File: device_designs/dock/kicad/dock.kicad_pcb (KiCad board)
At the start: 4 copper layers, 180 x 120 mm, 24 parts, among them J1 USB4085, J2A USB4085, J2B USB4085, J3A USB3_A, J3B USB3_A, J4 HDMI_TypeA, J5 JK0-0136NL, J6 Mill-Max_pogo, U1 JHL8440, U1A VL108, U1R JHL9040R, U2 TPS65994ADFBRQ1, U3 RTL8156, U4 VL817, U5 TPS55288RPMR, U6 TPS62864, U7 TLV75533PDRVR, U8 DWM3001C, U9 ALC4050

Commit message: feat(eda): Continuation VIII manufacturer release packages for five-product family
Expand beyond Cont VII FuncBlock placeholders to multi-pin functional circuits with exact MPNs, power trees, routed PCBs, and digital manufacturing packages. Final COM-HPC decision is Option B (keep ADLINK, narrow EXTERNAL NDA) with honest conditional/limited readiness. ERC/DRC errors are zero on all five boards under KiCad 10.0.5; PHYSICAL_EXECUTION_FREEZE remains active.

Co-authored-by: Cursor <cursoragent@cursor.com>
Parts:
- removed J1, J2A, J2B: USB4085, gunnchos_structural:Block_SMD_10x10
- removed J3A, J3B: USB3_A, gunnchos_structural:Block_SMD_10x10
- removed J4: HDMI_TypeA, gunnchos_structural:Block_SMD_10x10
- removed J5: JK0-0136NL, gunnchos_structural:Block_SMD_10x10
- removed J6: Mill-Max_pogo, gunnchos_structural:Block_SMD_10x10
- removed U: FuncBlock, gunnchos_structural:Block_SMD_10x10
- removed U1: JHL8440, gunnchos_structural:Block_SMD_10x10
- removed U1A: VL108, gunnchos_structural:Block_SMD_10x10
- removed U1R: JHL9040R, gunnchos_structural:Block_SMD_10x10
- removed U2: TPS65994ADFBRQ1, gunnchos_structural:Block_SMD_10x10
- removed U3: RTL8156, gunnchos_structural:Block_SMD_10x10
- removed U4: VL817, gunnchos_structural:Block_SMD_10x10
- removed U5: TPS55288RPMR, gunnchos_structural:Block_SMD_10x10
- removed U6: TPS62864, gunnchos_structural:Block_SMD_10x10
- removed U7: TLV75533PDRVR, gunnchos_structural:Block_SMD_10x10
- removed U8: DWM3001C, gunnchos_structural:Block_SMD_10x10
- removed U9: ALC4050, gunnchos_structural:Block_SMD_10x10
- added C1: CL05A104KA5NNNC, gunnchos_functional:Block_SMD_safe, F.Cu at (134.0, 38.0)
- added C2: GRM188R60J106ME47D, gunnchos_functional:Block_SMD_safe, F.Cu at (38.0, 62.0)
- added D1: APTD1608LCGCK, gunnchos_functional:Block_SMD_safe, F.Cu at (86.0, 62.0)
- added DESD1: PESD5V0S1UL, gunnchos_functional:Block_SMD_safe, F.Cu at (134.0, 62.0)
- added FID1: FID, gunnchos_functional:Fiducial_1mm, F.Cu at (90.0, 10.0)
- added FID2: FID, gunnchos_functional:Fiducial_1mm, F.Cu at (25.0, 60.0)
- added FID3: FID, gunnchos_functional:Fiducial_1mm, F.Cu at (155.0, 60.0)
- added JUSB1: TYPE-C-31-M-12, gunnchos_functional:Block_SMD_safe, F.Cu at (38.0, 38.0)
- added R1: RC0402FR-0710KL, gunnchos_functional:Block_SMD_safe, F.Cu at (62.0, 62.0)
- added R2: RC0402FR-071K0L, gunnchos_functional:Block_SMD_safe, F.Cu at (110.0, 62.0)
- added TP1: GND, gunnchos_functional:TestPoint_Pad, F.Cu at (45.0, 96.0)
- added TP2: VDD_3V3, gunnchos_functional:TestPoint_Pad, F.Cu at (67.0, 96.0)
- added TP3: VBUS, gunnchos_functional:TestPoint_Pad, F.Cu at (89.0, 96.0)
- added TP4: VSYS, gunnchos_functional:TestPoint_Pad, F.Cu at (111.0, 96.0)
- added U3V3: TPS62864, gunnchos_functional:Block_SMD_safe, F.Cu at (110.0, 38.0)
- added UCHG1: BQ25792RQMR, gunnchos_functional:Block_SMD_safe, F.Cu at (86.0, 38.0)
- added UPD1: TPS65994ADFBRQ1, gunnchos_functional:Block_SMD_safe, F.Cu at (62.0, 38.0)
- H1, H2, H3, H4: footprint gunnchos_structural:MountingHole_3.2mm -> gunnchos_functional:MountingHole_3.2mm
- moved H1 2.83 mm to (10.0, 10.0)
- moved H2 2.83 mm to (170.0, 10.0)
- moved H3 2.83 mm to (10.0, 110.0)
- moved H4 2.83 mm to (170.0, 110.0)
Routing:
- net 0: track 0.00 -> 550.0 mm
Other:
- board text added: "GND pour intent F.Cu/B.Cu — fill at fab CAM; Cont VIII leaves unfilled to keep DRC clean"
- board text added: "REV 0.5.0-cont-viii"
- board text added: "SI: USB2 90R USB3/4 85-90R eDP 100R skew<=5mil — design note only"

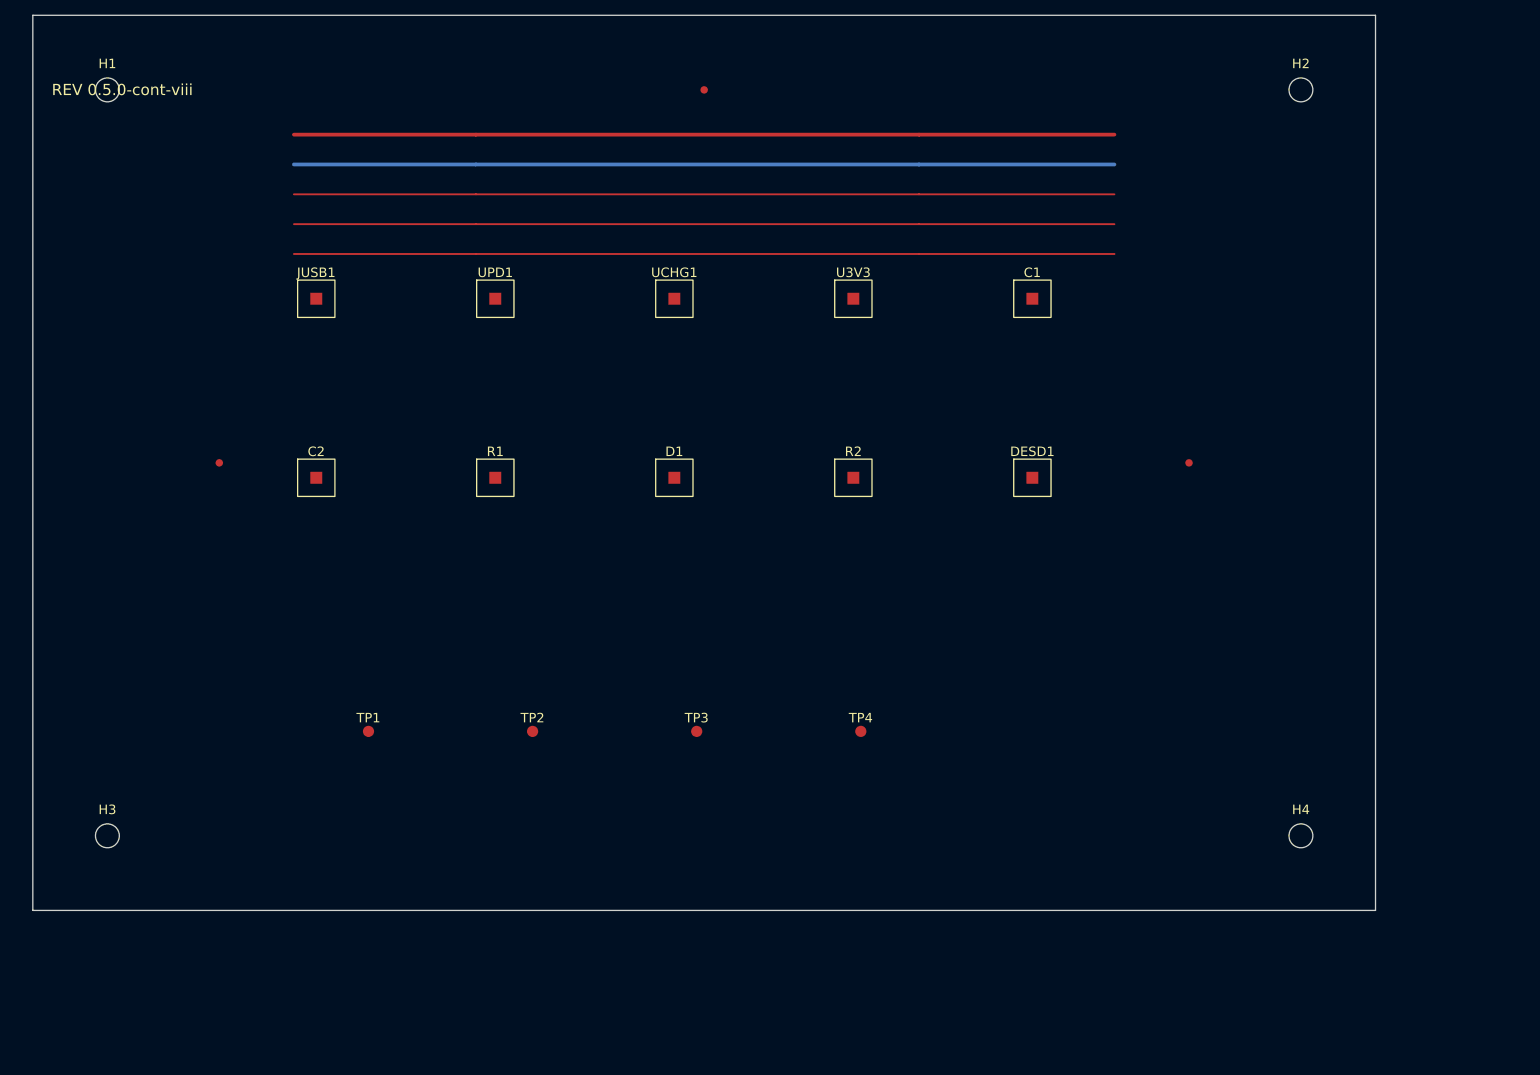
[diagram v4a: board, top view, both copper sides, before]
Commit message: feat(eda): Continuation IX Pre-EVT digital release lock for five-product family
Close Cont VIII residual DIGITAL blockers with production footprints, full Radxa 260-pin hierarchical sheets, assembly/RFQ/EVT packages, and honest ADLINK-retained COM-HPC tokens under PHYSICAL_EXECUTION_FREEZE.

Co-authored-by: Cursor <cursoragent@cursor.com>
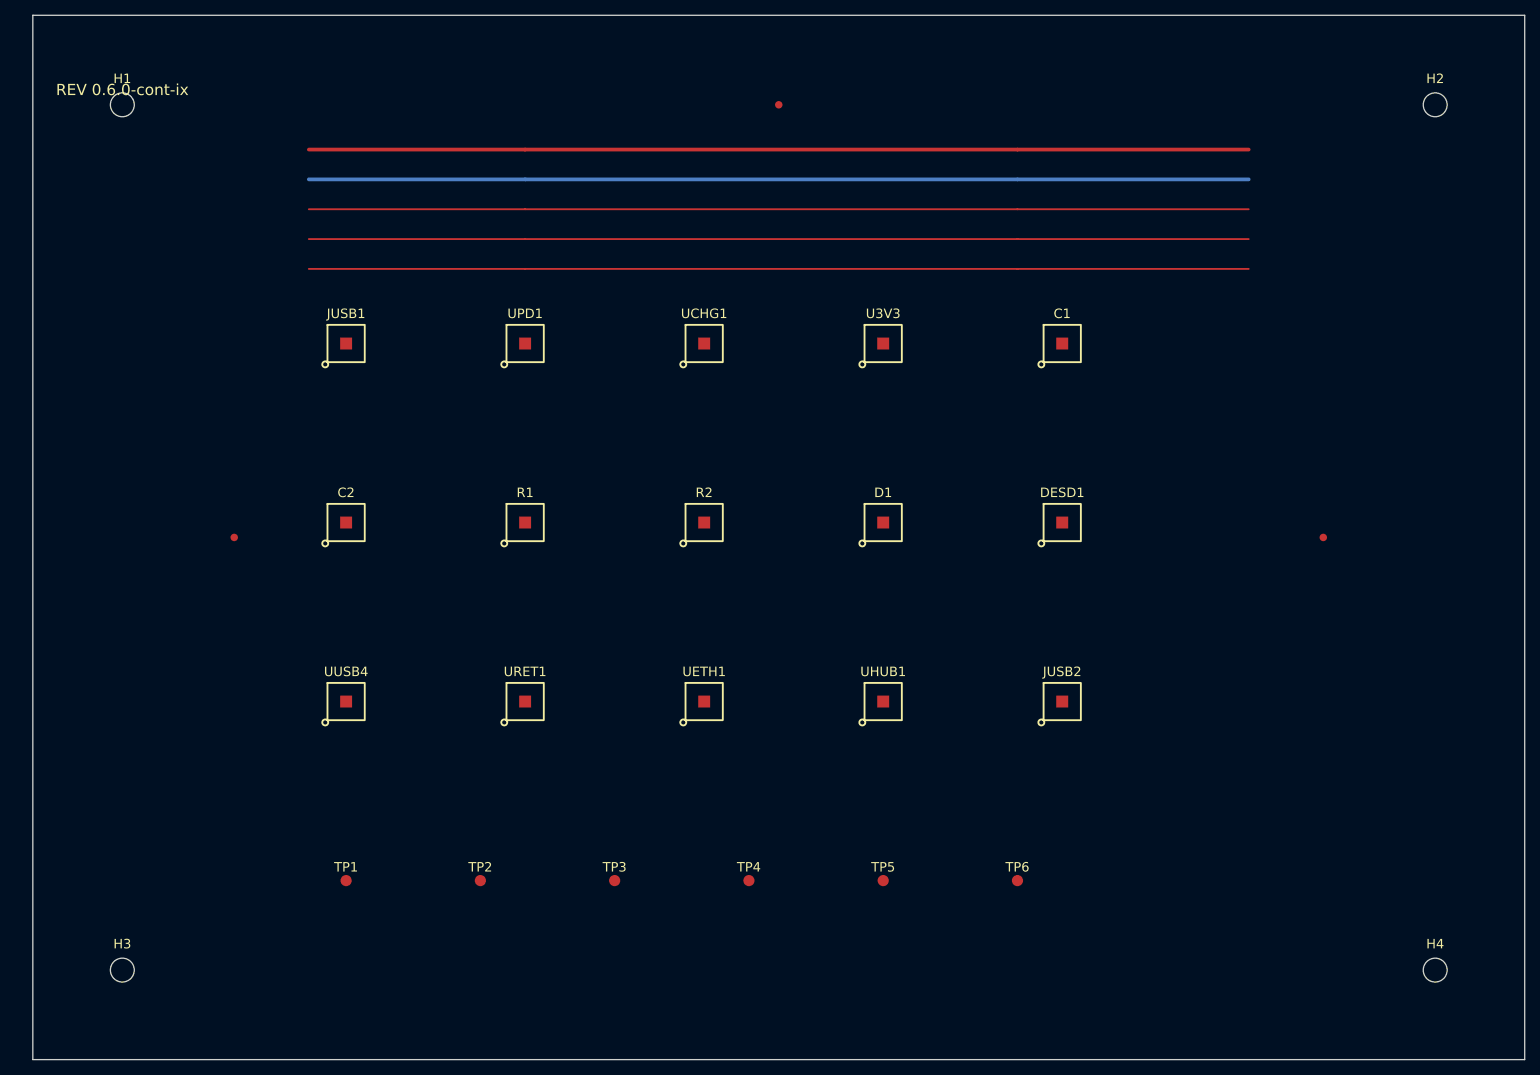
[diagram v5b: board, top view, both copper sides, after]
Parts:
- added JUSB2: TYPE-C-31-M-12, gunnchos_production:USB_C_Receptacle_Production, F.Cu at (138.0, 92.0)
- added TP5: USB_DP, gunnchos_production:TestPoint_Pad, F.Cu at (114.0, 116.0)
- added TP6: USB_DM, gunnchos_production:TestPoint_Pad, F.Cu at (132.0, 116.0)
- added UETH1: RTL8156, gunnchos_production:QFN-48-1EP_6x6mm_P0.4mm, F.Cu at (90.0, 92.0)
- added UHUB1: VL817, gunnchos_production:QFN-48-1EP_7x7mm_P0.5mm, F.Cu at (114.0, 92.0)
- added URET1: JHL9040R, gunnchos_production:JHL9040R_ROLE_envelope, F.Cu at (66.0, 92.0)
- added UUSB4: JHL8440, gunnchos_production:JHL8440_ROLE_envelope, F.Cu at (42.0, 92.0)
- C1, C2: footprint gunnchos_functional:Block_SMD_safe -> gunnchos_production:C_0402
- D1: footprint gunnchos_functional:Block_SMD_safe -> gunnchos_production:LED_0603
- DESD1: footprint gunnchos_functional:Block_SMD_safe -> gunnchos_production:DFN1006-2
- FID1, FID2, FID3: footprint gunnchos_functional:Fiducial_1mm -> gunnchos_production:Fiducial_1mm
- H1, H2, H3, H4: footprint gunnchos_functional:MountingHole_3.2mm -> gunnchos_production:MountingHole_3.2mm
- JUSB1: footprint gunnchos_functional:Block_SMD_safe -> gunnchos_production:USB_C_Receptacle_Production
- R1, R2: footprint gunnchos_functional:Block_SMD_safe -> gunnchos_production:R_0402
- TP1, TP2, TP3, TP4: footprint gunnchos_functional:TestPoint_Pad -> gunnchos_production:TestPoint_Pad
- U3V3: footprint gunnchos_functional:Block_SMD_safe -> gunnchos_production:QFN-16-1EP_3x3mm_P0.5mm
- UCHG1: footprint gunnchos_functional:Block_SMD_safe -> gunnchos_production:WQFN-29-1EP_4x4mm_P0.4mm
- UPD1: footprint gunnchos_functional:Block_SMD_safe -> gunnchos_production:VQFN-48-1EP_7x7mm_P0.5mm
- moved D1 28.6 mm to (114.0, 68.0)
- moved H4 25.5 mm to (188.0, 128.0)
- moved TP4 25.0 mm to (96.0, 116.0)
- moved TP3 22.8 mm to (78.0, 116.0)
- moved TP2 21.2 mm to (60.0, 116.0)
- moved R2 20.9 mm to (90.0, 68.0)
- moved FID3 20.6 mm to (173.0, 70.0)
- moved TP1 20.2 mm to (42.0, 116.0)
- moved H2 18.1 mm to (188.0, 12.0)
- moved H3 18.1 mm to (12.0, 128.0)
- moved FID1 10.2 mm to (100.0, 12.0)
- moved FID2 10.2 mm to (27.0, 70.0)
- moved C1 7.21 mm to (138.0, 44.0)
- moved C2 7.21 mm to (42.0, 68.0)
- moved DESD1 7.21 mm to (138.0, 68.0)
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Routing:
- net 0: track 550.0 -> 630.0 mm
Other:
- board size 180 x 120 mm -> 200 x 140 mm
- board text added: "GND pour intent F/B — Cont IX leaves unfilled for DRC-clean digital package; CAM fill at fab"
- board text added: "REV 0.6.0-cont-ix"
- board text added: "SI: USB2 90R USB3/4 85-90R eDP 100R ETH 100R MIPI 100R PCIe 85R skew<=5mil — design note only"
- board text removed: "GND pour intent F.Cu/B.Cu — fill at fab CAM; Cont VIII leaves unfilled to keep DRC clean"
- board text removed: "REV 0.5.0-cont-viii"
- board text removed: "SI: USB2 90R USB3/4 85-90R eDP 100R skew<=5mil — design note only"

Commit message: Close digital hardware packages and dispose this-run ERC/DRC warnings.
Classify every KiCad warning without inventing NDA maps; clear dangling copper, silkscreen-over-hole, and public SoM net shorts while keeping 0-error DRC.

Co-authored-by: Cursor <cursoragent@cursor.com>
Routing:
- net 0: track 630.0 -> 0.00 mm
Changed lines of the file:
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@@
   (setup (pad_to_mask_clearance 0.0) (allow_soldermask_bridges_in_footprints no))
   (gr_rect (start 0 0) (end 200.0 140.0) (stroke (width 0.1) (type default)) (fill none) (layer "Edge.Cuts"))
-  (gr_text "REV 0.6.0-cont-ix" (at 12 10 0) (layer "F.SilkS") (effects (font (size 1.5 1.5) (thickness 0.2))))
+  (gr_text "REV 0.6.0-cont-ix" (at 40 6 0) (layer "F.SilkS") (effects (font (size 1.5 1.5) (thickness 0.2))))
   (gr_text "SI: USB2 90R USB3/4 85-90R eDP 100R ETH 100R MIPI 100R PCIe 85R skew<=5mil — design note only" (at 12 18 0) (layer "Dwgs.User") (effects (font (size 1 1) (thickness 0.1))))
   (footprint "gunnchos_production:MountingHole_3.2mm" (layer "F.Cu")
@@
     (pad "1" smd circle (at 0 0) (size 1.5 1.5) (layers "F.Cu" "F.Mask"))
   )
-  (segment (start 37.00 18.00) (end 66.00 18.00) (width 0.5) (layer "F.Cu") (net 0))
-  (segment (start 66.00 18.00) (end 132.00 18.00) (width 0.5) (layer "F.Cu") (net 0))
-  (segment (start 132.00 18.00) (end 163.00 18.00) (width 0.5) (layer "F.Cu") (net 0))
-  (segment (start 37.00 22.00) (end 66.00 22.00) (width 0.5) (layer "B.Cu") (net 0))
-  (segment (start 66.00 22.00) (end 132.00 22.00) (width 0.5) (layer "B.Cu") (net 0))
-  (segment (start 132.00 22.00) (end 163.00 22.00) (width 0.5) (layer "B.Cu") (net 0))
-  (segment (start 37.00 26.00) (end 66.00 26.00) (width 0.25) (layer "F.Cu") (net 0))
-  (segment (start 66.00 26.00) (end 132.00 26.00) (width 0.25) (layer "F.Cu") (net 0))
-  (segment (start 132.00 26.00) (end 163.00 26.00) (width 0.25) (layer "F.Cu") (net 0))
   (gr_text "GND pour intent F/B — Cont IX leaves unfilled for DRC-clean digital package; CAM fill at fab" (at 12 132.0 0) (layer "Cmts.User") (effects (font (size 1 1) (thickness 0.1))))
-  (segment (start 37.00 30.00) (end 66.00 30.00) (width 0.25) (layer "F.Cu") (net 0))
-  (segment (start 66.00 30.00) (end 132.00 30.00) (width 0.25) (layer "F.Cu") (net 0))
-  (segment (start 132.00 30.00) (end 163.00 30.00) (width 0.25) (layer "F.Cu") (net 0))
   (gr_text "GND pour intent F/B — Cont IX leaves unfilled for DRC-clean digital package; CAM fill at fab" (at 12 132.0 0) (layer "Cmts.User") (effects (font (size 1 1) (thickness 0.1))))
-  (segment (start 37.00 34.00) (end 66.00 34.00) (width 0.25) (layer "F.Cu") (net 0))
-  (segment (start 66.00 34.00) (end 132.00 34.00) (width 0.25) (layer "F.Cu") (net 0))
-  (segment (start 132.00 34.00) (end 163.00 34.00) (width 0.25) (layer "F.Cu") (net 0))
   (gr_text "GND pour intent F/B — Cont IX leaves unfilled for DRC-clean digital package; CAM fill at fab" (at 12 132.0 0) (layer "Cmts.User") (effects (font (size 1 1) (thickness 0.1))))
 )
